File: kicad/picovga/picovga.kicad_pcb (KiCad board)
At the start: 2 copper layers, 31.1 x 62.5 mm, 26 parts, among them J0 VGA_FEMALE, J1 Micro_SD_Card, U0 PICO_RP2040, U1 PCA9306DC

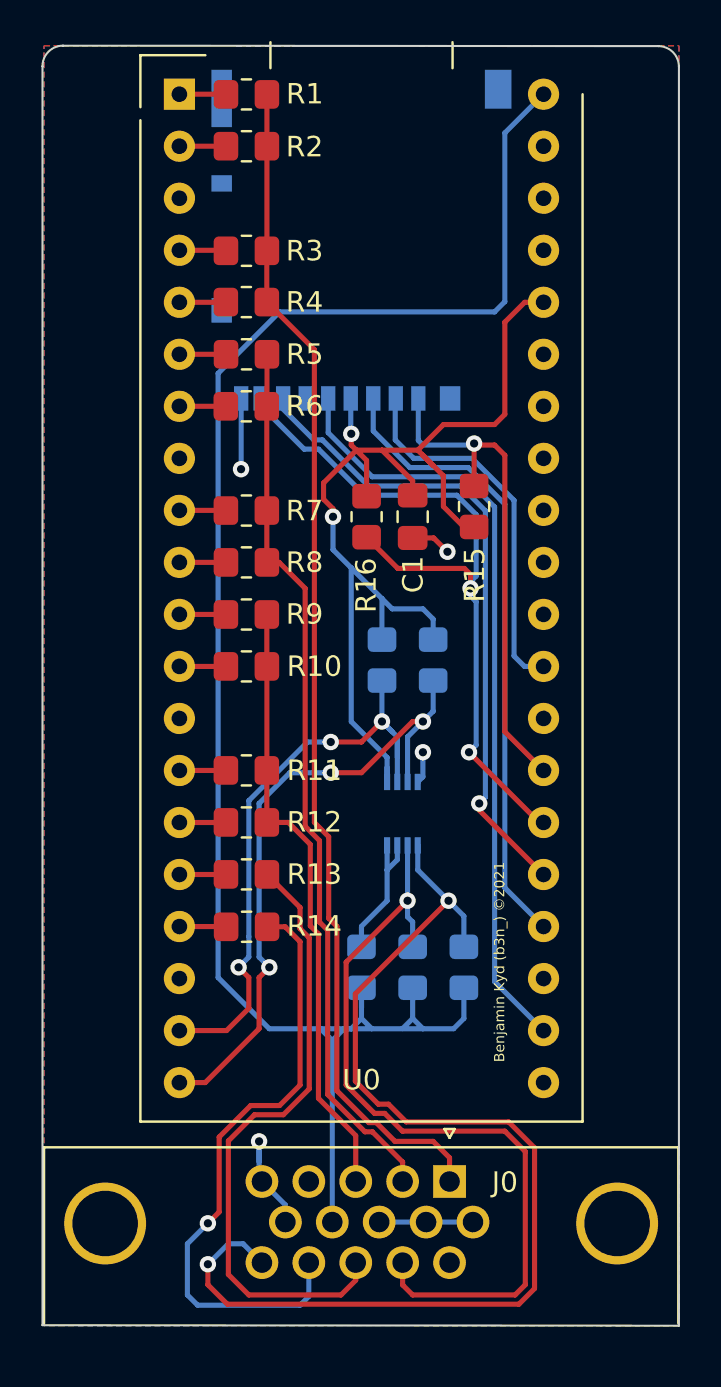
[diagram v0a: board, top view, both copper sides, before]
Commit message: board off for fabrication
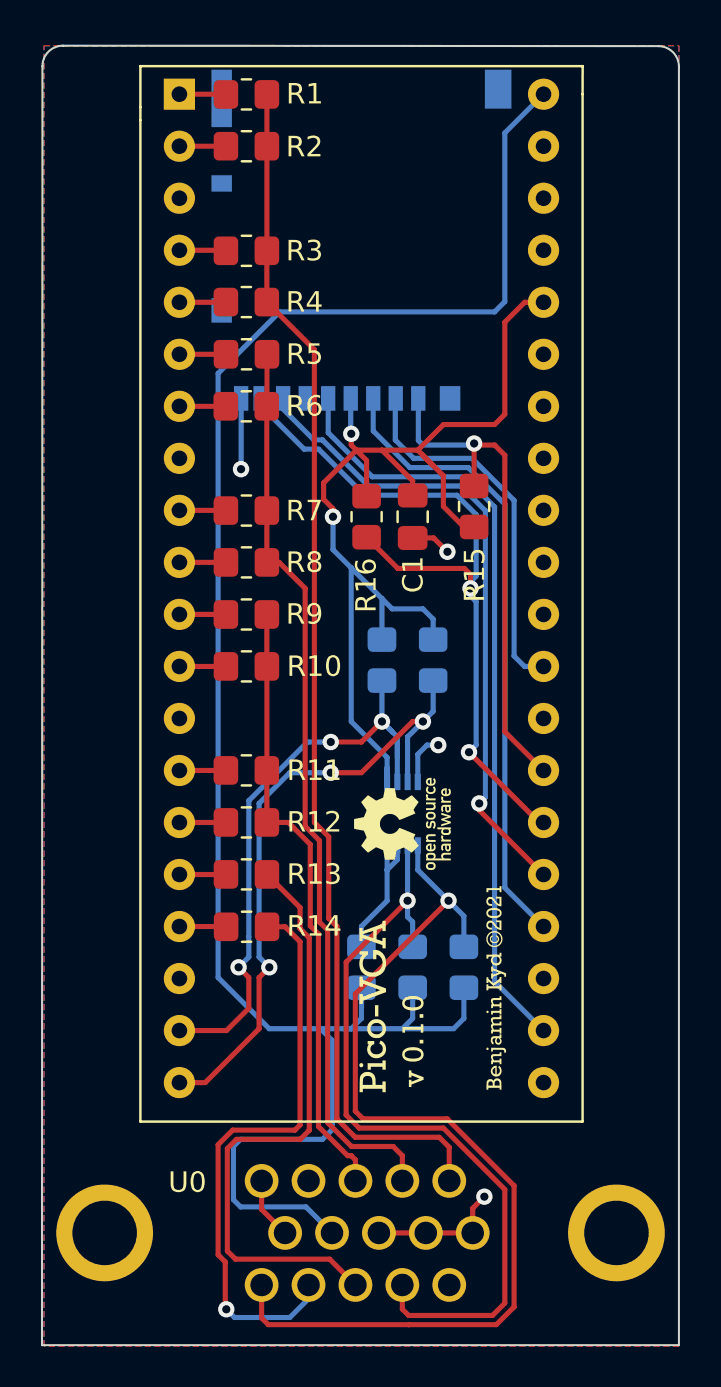
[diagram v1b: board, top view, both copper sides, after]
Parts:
- added ?: LOGO, pico:osh, F.Cu at (171.0, 98.5)
- added G: LOGO, kiwih_kicad:name-logo, F.Cu at (175.5, 106.5)
- added G: LOGO, kiwih_kicad:product-version, F.Cu at (171.5, 109.0)
- added G: LOGO, kiwih_kicad:product-logo, F.Cu at (169.5, 107.5)
- J0: footprint Connector_Dsub:DSUB-15-HD_Female_Horizontal_P2.29x1.98mm_EdgePinOffset3.03mm_Housed_MountingHolesOffset4.94mm -> pico:XM4L1542132; moved to B.Cu
- moved J0 7.20 mm to (169.0, 121.7)
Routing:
- net DCC5VCLK: track 54.6 -> 47.7 mm, vias 2 -> 1
- net +5V: track 88.3 -> 94.8 mm
- net VSYNC: track 30.2 -> 28.7 mm
- net VGA_R: track 58.1 -> 59.1 mm
- net HSYNC: track 30.6 -> 29.7 mm
- net VGA_G: track 43.7 -> 44.6 mm
- net GND: track 17.0 -> 17.8 mm
- net DCC5VDAT: track 39.4 -> 38.8 mm
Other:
- board size 31.1 x 62.5 mm -> 31.1 x 63.5 mm
- board text removed: "Benjamin Kyd (b3n_) ©2021"
